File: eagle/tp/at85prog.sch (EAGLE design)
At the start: 6 parts, among them J1 ICSP, U1 TINY45-20-DIP

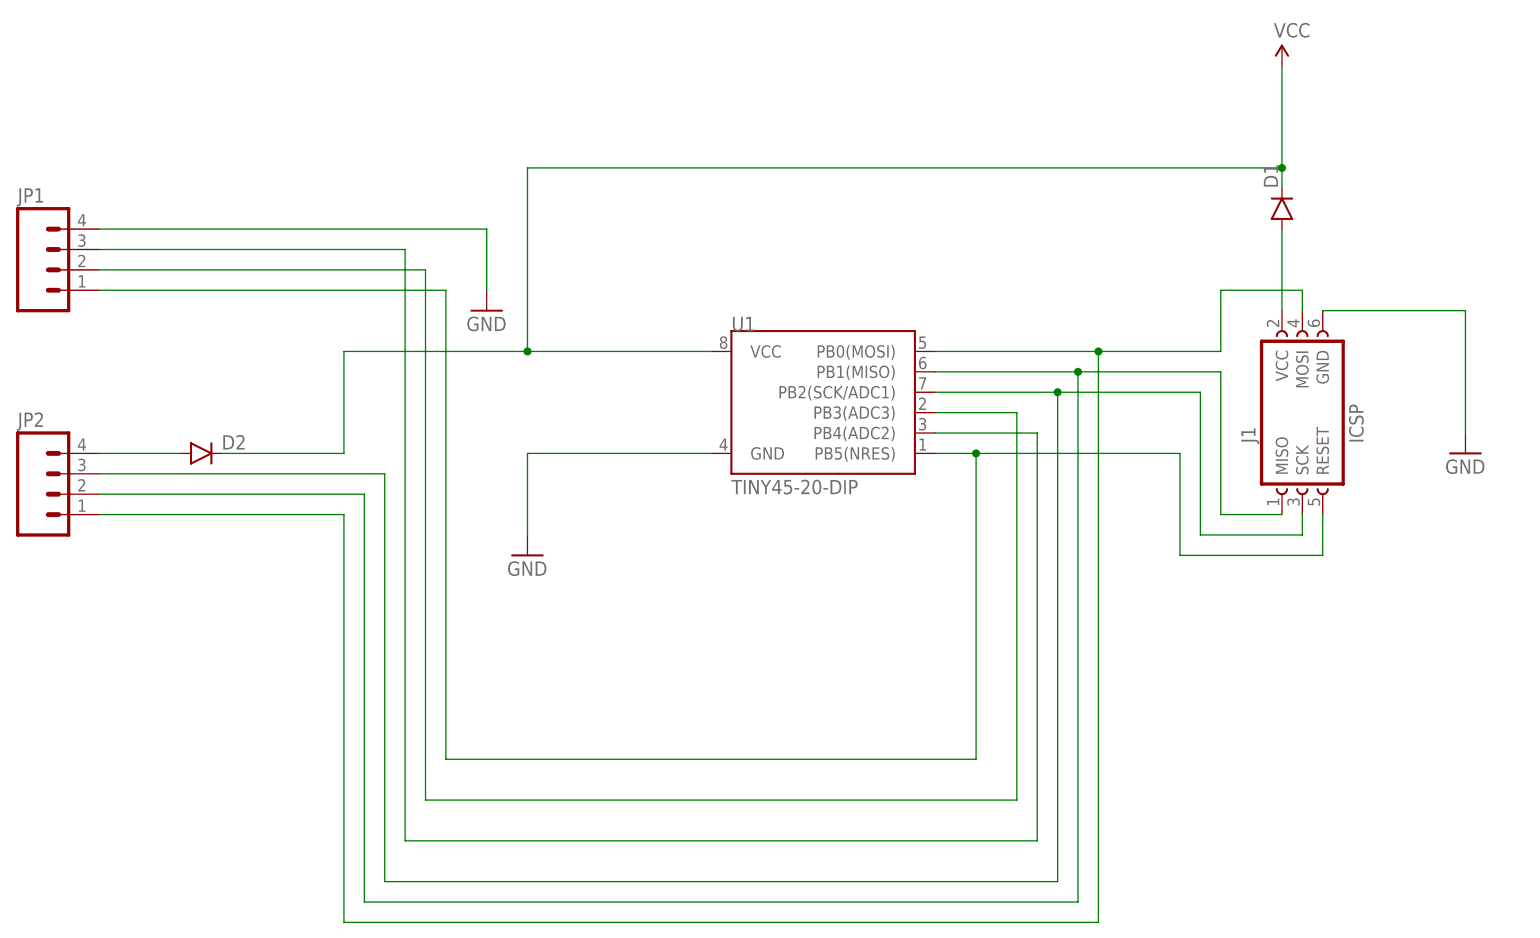
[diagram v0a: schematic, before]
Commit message: tp: add reset button.
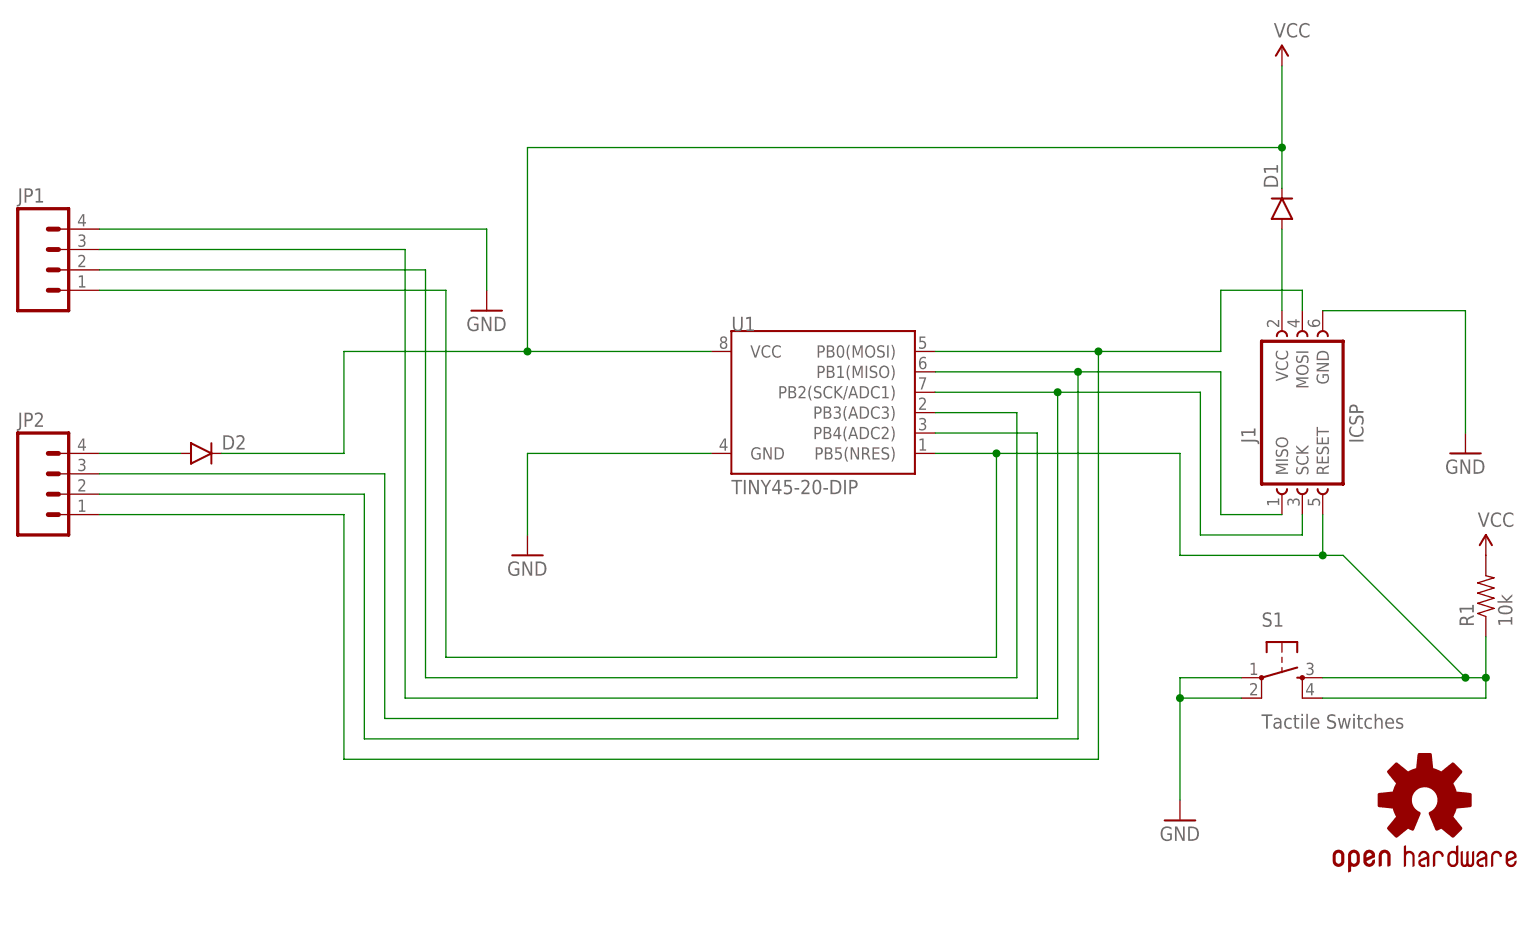
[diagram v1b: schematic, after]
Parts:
- added LOGO1: OSHW-LOGOS, SparkFun-Aesthetics:OSHW-LOGOS
- added R1: 10k, SparkFun-Passives:RESISTOR1206
- added S1: Tactile Switches, gipi:TAC_SWITCHSMD
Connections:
- net GND: now also S1.1, S1.2
- net N$4: now also R1.1, S1.3, S1.4
- net VCC: now also R1.2
